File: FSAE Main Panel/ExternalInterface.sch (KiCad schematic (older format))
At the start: 10 parts, among them J1 Conn_01x04, J2 TE_84953-6_FPC, SW1 B3W-1020, SW2 B3W-1020

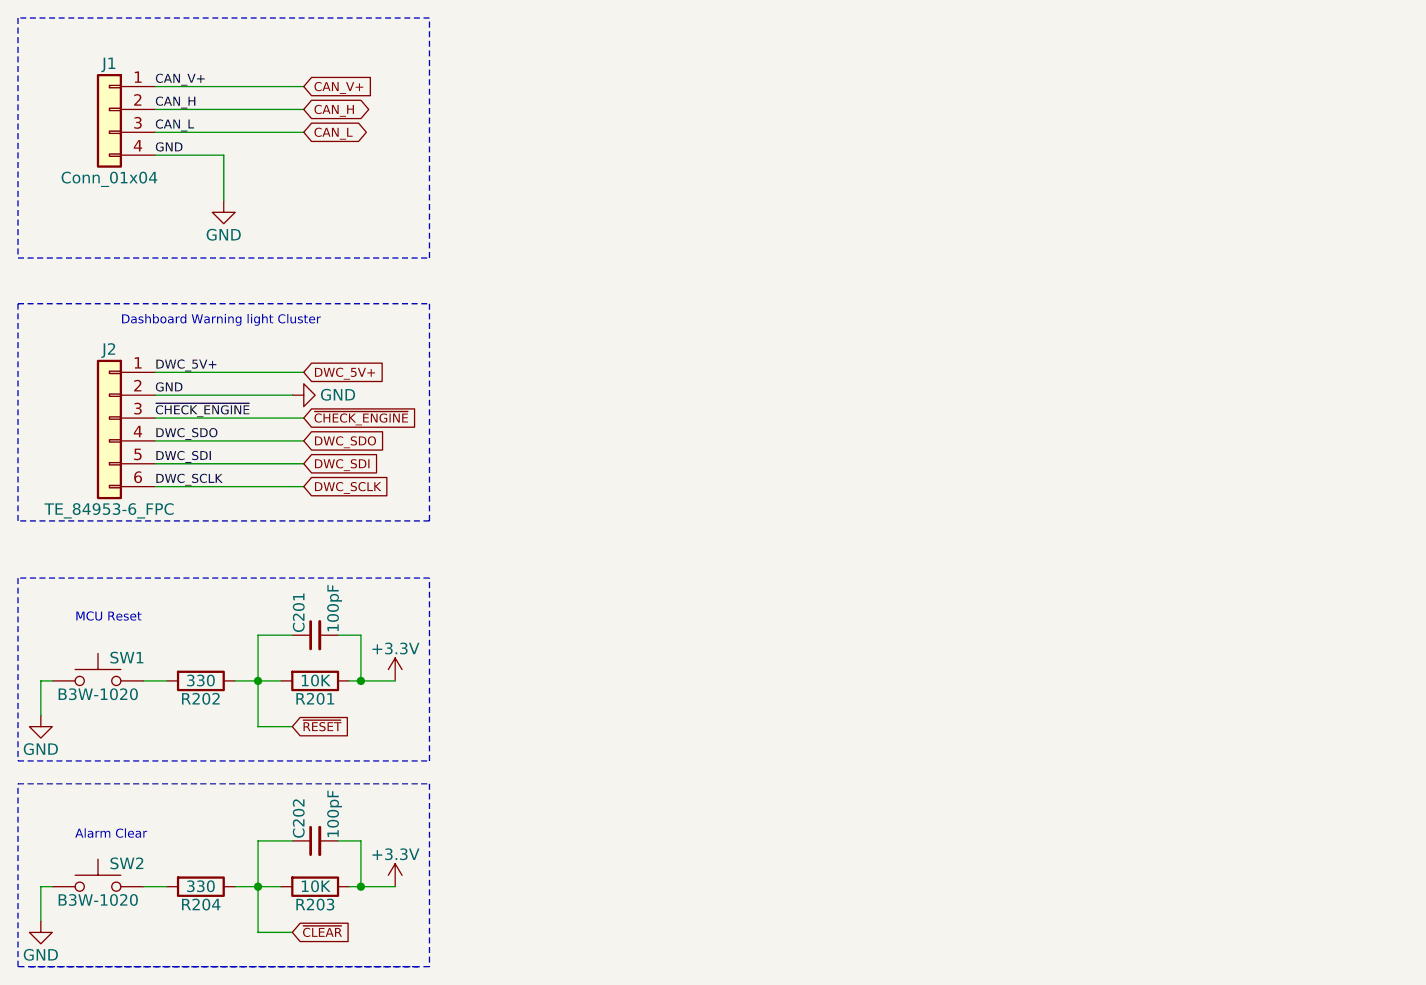
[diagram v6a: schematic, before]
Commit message: Moved USB connection to External_Interface
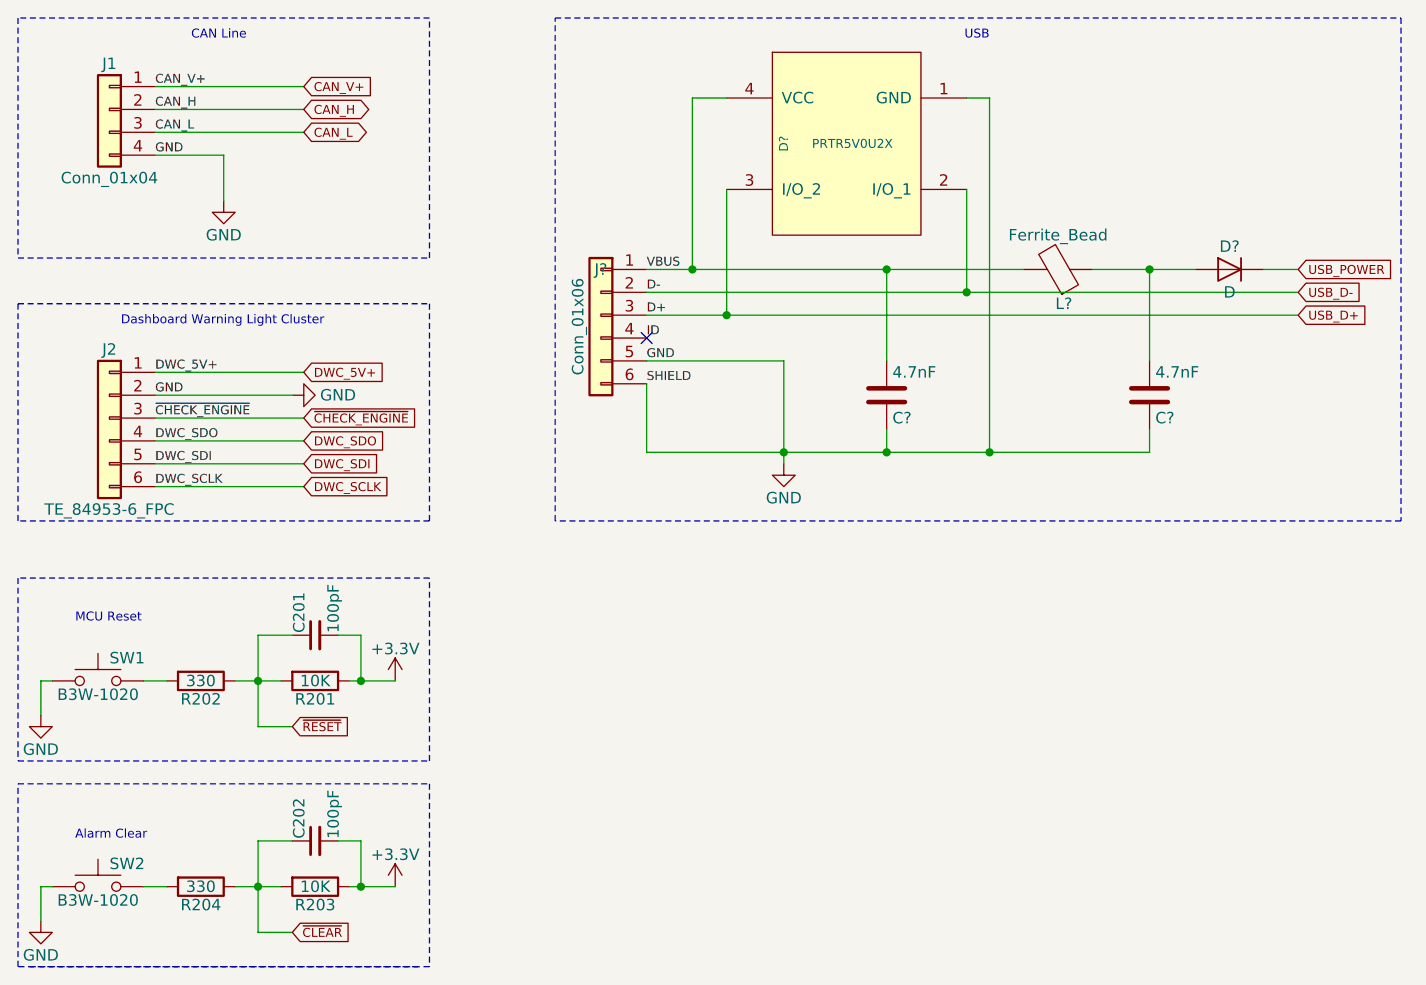
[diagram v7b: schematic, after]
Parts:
- added C? (x2): 4.7nF, symbol C
- added D?: D, symbol D
- added D?: PRTR5V0U2X, symbol PRTR5V0U2X
- added J?: Conn_01x06, symbol Conn_01x06
- added L?: Ferrite_Bead, symbol Ferrite_Bead
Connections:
- net GND: now also C?.1, C?.1, D?.1 (GND), J?.5 (Pin_5), J?.6 (Pin_6)
- new net: C?.2, D?.2 (A), L?.1
- new net ID: J?.4 (Pin_4)
- new net USB_D+: D?.3 (I/O_2), J?.3 (Pin_3)
- new net USB_D-: D?.2 (I/O_1), J?.2 (Pin_2)
- new net USB_POWER: D?.1 (K)
- new net VBUS: C?.2, D?.4 (VCC), J?.1 (Pin_1), L?.2
- no-connect marks 0 -> 1
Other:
- note added: "CAN Line"
- note added: "Dashboard Warning Light Cluster"
- note added: "USB"
- note removed: "Dashboard Warning light Cluster"
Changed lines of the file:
@@
 DWC_SCLK
 Text Notes 1100 2200 0    39   ~ 0
-Dashboard Warning light Cluster
+Dashboard Warning Light Cluster
 Wire Notes Line
 	650  2100 2450 2100
@@
 	1    0    0    -1
 $EndComp
+$Comp
+L Conn_01x06 J?
+U 1 1 5BF06479
+P 3200 2150
+F 0 "J?" H 3200 2350 50  0000 C CNN
+F 1 "Conn_01x06" V 3300 2100 50  0000 C CNN
+F 2 "" H 3200 2150 50  0001 C CNN
+F 3 "" H 3200 2150 50  0001 C CNN
+	1    3200 2150
+	-1   0    0    -1
+$EndComp
+$Comp
+L GND #PWR?
+U 1 1 5BF06480
+P 4000 2800
+F 0 "#PWR?" H 4000 2550 50  0001 C CNN
+F 1 "GND" H 4000 2650 50  0000 C CNN
+F 2 "" H 4000 2800 50  0001 C CNN
+F 3 "" H 4000 2800 50  0001 C CNN
+	1    4000 2800
+	-1   0    0    -1
+$EndComp
+$Comp
+L Ferrite_Bead L?
+U 1 1 5BF06486
+P 5200 1950
+F 0 "L?" V 5050 1975 50  0000 C CNN
+F 1 "Ferrite_Bead" V 5350 1950 50  0000 C CNN
+F 2 "" V 5130 1950 50  0001 C CNN
+F 3 "" H 5200 1950 50  0001 C CNN
+	1    5200 1950
+	0    1    -1   0
+$EndComp
+$Comp
+L D D?
+U 1 1 5BF0648D
+P 5950 1950
+F 0 "D?" H 5950 2050 50  0000 C CNN
+F 1 "D" H 5950 1850 50  0000 C CNN
+F 2 "" H 5950 1950 50  0001 C CNN
+F 3 "" H 5950 1950 50  0001 C CNN
+	1    5950 1950
+	-1   0    0    -1
+$EndComp
+$Comp
+L C C?
+U 1 1 5BF06494
+P 4450 2500
+F 0 "C?" H 4475 2600 50  0000 L CNN
+F 1 "4.7nF" H 4475 2400 50  0000 L CNN
+F 2 "" H 4488 2350 50  0001 C CNN
+F 3 "" H 4450 2500 50  0001 C CNN
+	1    4450 2500
+	1    0    0    1
+$EndComp
+$Comp
+L PRTR5V0U2X D?
+U 1 1 5BF064A8
+P 4300 1400
+F 0 "D?" H 4300 1700 39  0000 C CNN
+F 1 "PRTR5V0U2X" V 4300 1400 39  0000 C CNN
+F 2 "" H 4300 1400 60  0001 C CNN
+F 3 "" H 4300 1400 60  0001 C CNN
+	1    4300 1400
+	0    -1   1    0
+$EndComp
+Wire Wire Line
+	3400 1950 5050 1950
+Wire Wire Line
+	3400 2350 4000 2350
+Wire Wire Line
+	4000 2350 4000 2800
+Wire Wire Line
+	3400 2050 6250 2050
+Wire Wire Line
+	3750 1600 3750 2150
+Text Label 3400 1950 0    39   ~ 0
+VBUS
+Text Label 3400 2050 0    39   ~ 0
+D-
+Text Label 3400 2150 0    39   ~ 0
+D+
+Text Label 3400 2250 0    39   ~ 0
+ID
+Text Label 3400 2350 0    39   ~ 0
+GND
+Text Label 3400 2450 0    39   ~ 0
+SHIELD
+Text GLabel 6250 1950 2    39   Input ~ 0
+USB_POWER
+Connection ~ 3750 2150
+Wire Wire Line
+	3400 2150 6250 2150
+Wire Wire Line
+	3750 1200 3600 1200
+Wire Wire Line
+	3600 1200 3600 1950
+Connection ~ 3600 1950
+Wire Wire Line
+	5350 1950 5800 1950
+Wire Wire Line
+	4450 1950 4450 2350
+Connection ~ 4450 1950
+Wire Wire Line
+	5600 2350 5600 1950
+Connection ~ 5600 1950
+Wire Wire Line
+	6250 1950 6100 1950
+$Comp
+L C C?
+U 1 1 5BF0649B
+P 5600 2500
+F 0 "C?" H 5625 2600 50  0000 L CNN
+F 1 "4.7nF" H 5625 2400 50  0000 L CNN
+F 2 "" H 5638 2350 50  0001 C CNN
+F 3 "" H 5600 2500 50  0001 C CNN
+	1    5600 2500
+	1    0    0    1
+$EndComp
+Wire Wire Line
+	4800 2050 4800 1600
+Connection ~ 4800 2050
+Wire Wire Line
+	4800 1200 4900 1200
+Wire Wire Line
+	4900 1200 4900 2750
+Text GLabel 6250 2150 2    39   Input ~ 0
+USB_D+
+Text GLabel 6250 2050 2    39   Input ~ 0
+USB_D-
+Wire Wire Line
+	5600 2750 5600 2650
+Wire Wire Line
+	3400 2750 5600 2750
+Connection ~ 4000 2750
+Connection ~ 4900 2750
+Wire Wire Line
+	4450 2650 4450 2750
+Connection ~ 4450 2750
+Wire Notes Line
+	3000 850  6700 850
+Wire Notes Line
+	6700 850  6700 3050
+Wire Notes Line
+	6700 3050 3000 3050
+Wire Notes Line
+	3000 3050 3000 850
+Text Notes 1650 950  2    39   ~ 0
+CAN Line
+Text Notes 4900 950  2    39   ~ 0
+USB
+NoConn ~ 3400 2250
+Wire Wire Line
+	3400 2450 3400 2750
 $EndSCHEMATC

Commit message: Updated power circuit for MCU, used small components on main sheet
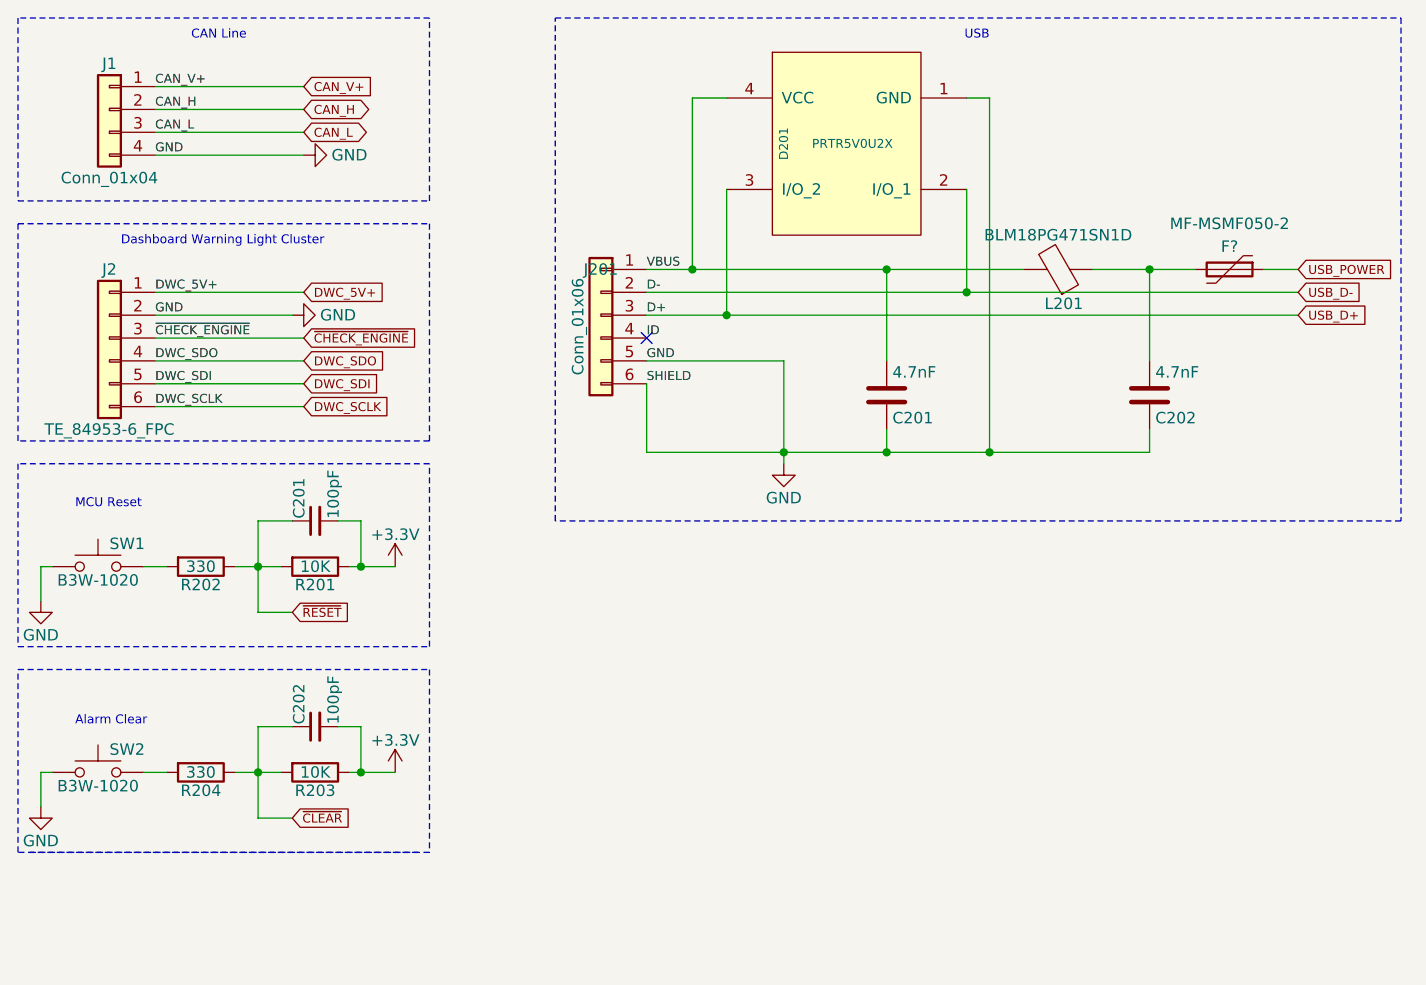
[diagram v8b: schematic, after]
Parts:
- removed D?: D, symbol D
- added F?: MF-MSMF050-2, symbol Polyfuse
- L201: renamed from L?; value Ferrite_Bead -> BLM18PG471SN1D
- gave numbers to parts that had none: 4
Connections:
- net USB_POWER: now also F?.1
- net at C202.2, L201.1: now also F?.2
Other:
- moved on the sheet: C201, C202, J2, R201, R202, R203, R204, SW1, SW2
